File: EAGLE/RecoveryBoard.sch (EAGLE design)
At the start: 54 parts, among them IC1 BD62120AEFJ-E2, Q6 MOSFET-PCH-SOT23-6, U1 STM32F042K6, U10 TPS63070, Y1 ECS-160-10-36Q-ES-TR

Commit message: updated gitignore finally working
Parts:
- added U$5: MP26123DR-LF-Z, U--MP26123DR-LF-Z--LiPo Charger:MP26123DR-LF-Z
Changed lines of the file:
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@@
 </part>
 <part name="GND3" library="supply1" deviceset="GND" device=""/>
+<part name="U$5" library="U--MP26123DR-LF-Z--LiPo Charger" deviceset="MP26123DR-LF-Z" device=""/>
 </parts>
 <sheets>
@@
 <attribute name="DRAWING_NAME" x="469.9" y="19.05" size="2.54" layer="94"/>
 </instance>
-<instance part="VUMB1" gate="1" x="312.42" y="254" smashed="yes">
-<attribute name="VALUE" x="309.88" y="248.92" size="1.778" layer="96" rot="R90"/>
+<instance part="VUMB1" gate="1" x="196.85" y="246.38" smashed="yes">
+<attribute name="VALUE" x="194.31" y="241.3" size="1.778" layer="96" rot="R90"/>
+</instance>
+<instance part="U$5" gate="G$1" x="233.68" y="223.52" smashed="yes">
+<attribute name="NAME" x="233.68" y="226.06" size="0.8128" layer="95" align="center"/>
+<attribute name="VALUE" x="233.68" y="223.52" size="0.8128" layer="96" align="center"/>
 </instance>
 </instances>

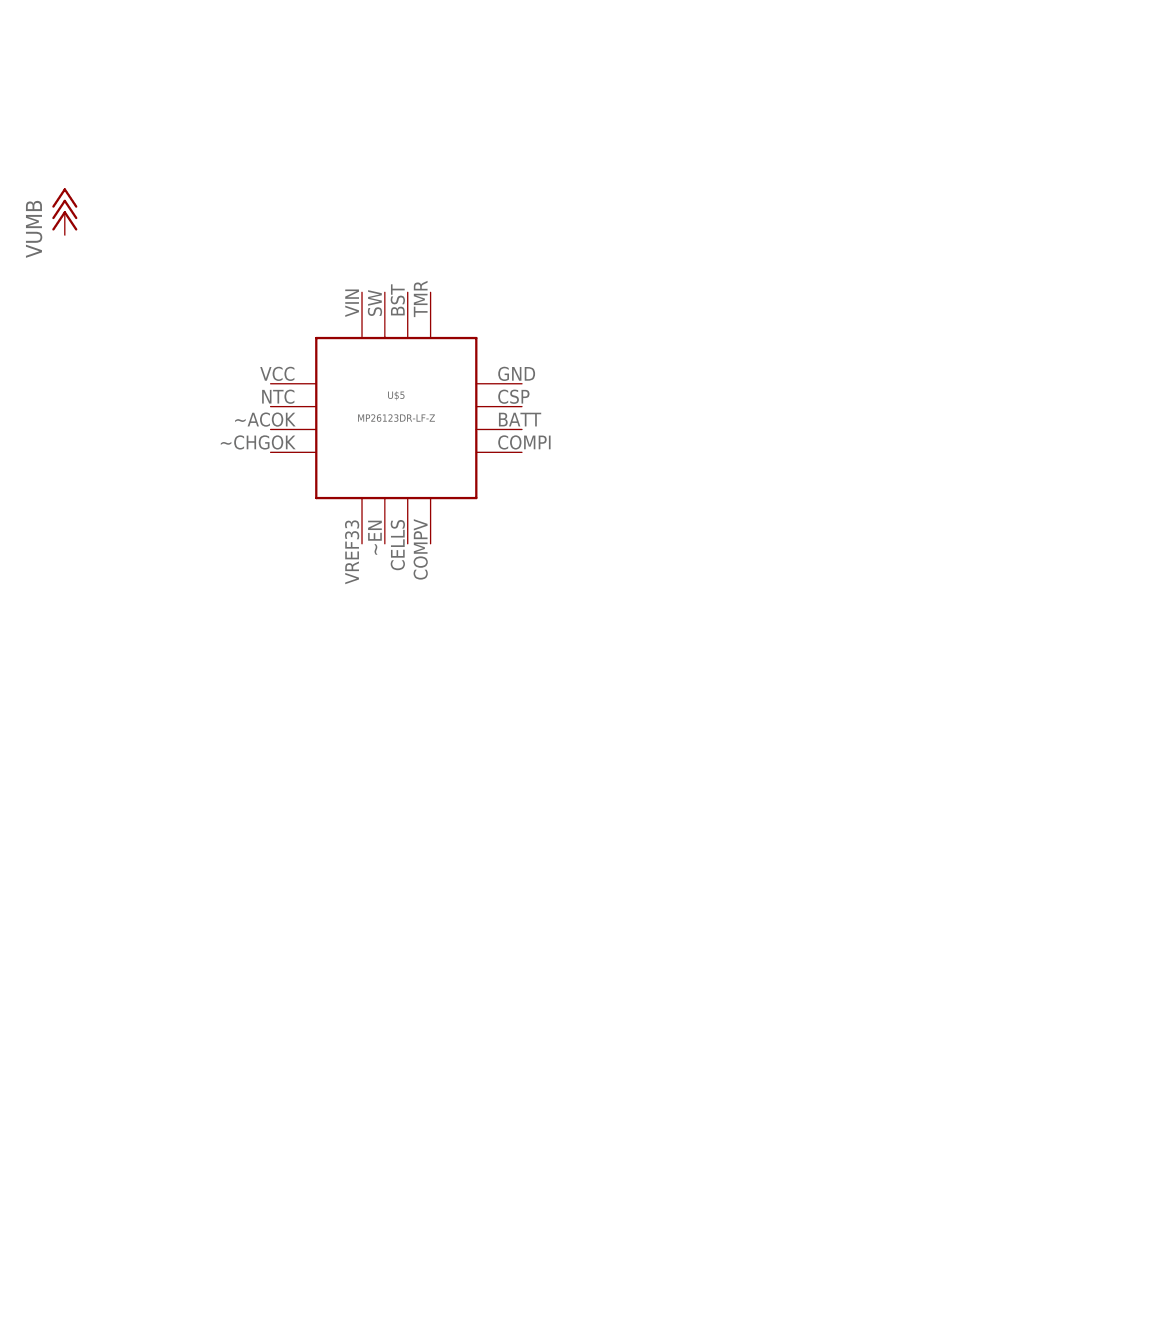
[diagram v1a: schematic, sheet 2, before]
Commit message: updated board to include LiPo charger, and the changes discussed after first design review
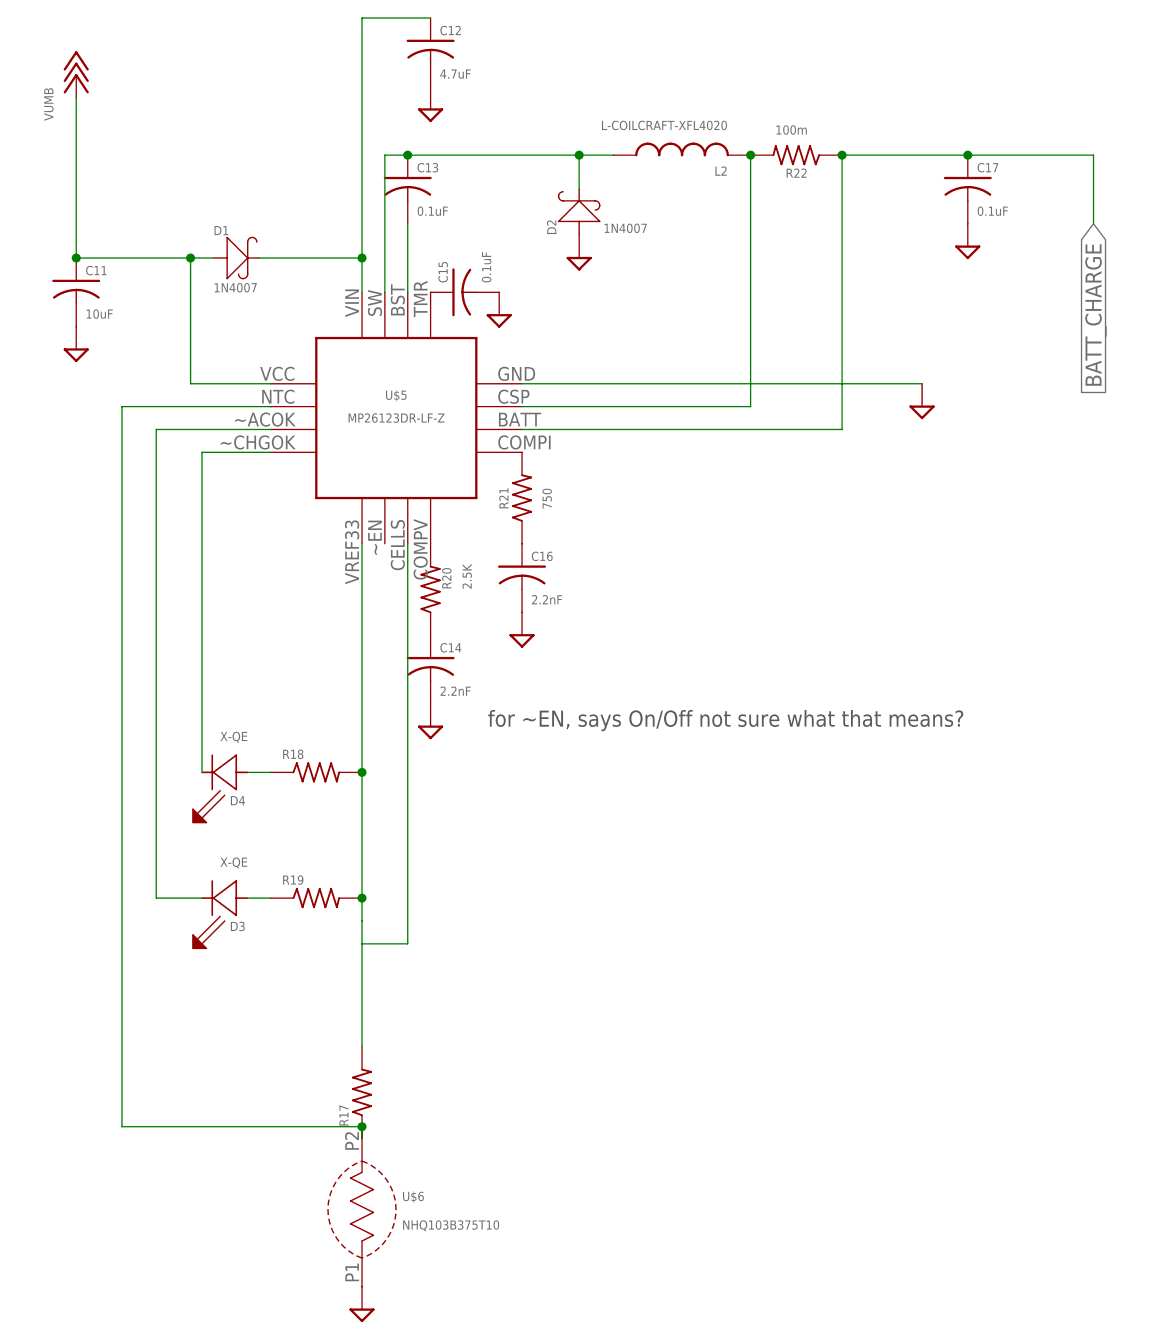
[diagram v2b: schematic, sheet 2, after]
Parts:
- added C11: 10uF, rcl:C-USC0402
- added C12: 4.7uF, rcl:C-USC0402
- added C13, C15, C17: 0.1uF, rcl:C-USC0402
- added C14, C16: 2.2nF, rcl:C-USC0402
- added D1, D2: 1N4007, D-Generic-Schottky-DO-214AC-SMA:DIODE-SCHOTTKY-(DO-214AC)
- added D3, D4: X-QE, D-Cree-XQE-LED:X-QE
- added L2: L-COILCRAFT-XFL4020, L-Coilcraft-XFL4020:L-COILCRAFT-XFL4020
- added R17, R18, R19: (no value), rcl:R-US_R0402
- added R20: 2.5K, rcl:R-US_R0402
- added R21: 750, rcl:R-US_R0402
- added R22: 100m, rcl:R-US_R0402
- added U$6: NHQ103B375T10, R--NHQ103B375T10--Thermistor:NHQ103B375T10
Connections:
- net DMC_ON renamed DCM_ON
- new net N$10: C13.1, D2.-, L2.1, U$5.SW
- new net N$11: C13.2, U$5.BST
- new net N$12: R17.1, U$5.NTC, U$6.P2
- new net N$13: D4.C, U$5.~CHGOK
- new net N$14: R17.2, R18.2, R19.2, U$5.CELLS, U$5.VREF33
- new net N$15: D3.C, U$5.~ACOK
- new net N$16: D3.A, R19.1
- new net N$17: D4.A, R18.1
- new net N$18: R20.2, U$5.COMPV
- new net N$19: C14.1, R20.1
- new net N$20: C15.1, U$5.TMR
- new net N$21: R21.2, U$5.COMPI
- new net N$22: C16.1, R21.1
- new net N$23: L2.2, R22.2, U$5.CSP
- new net N$9: C12.1, D1.-, U$5.VIN
- net +18V: now also C11.1, D1.+, U$5.VCC
- net BATT_CHARGE: now also C17.1, R22.1, U$5.BATT
- net GND: now also C11.2, C12.2, C14.2, C15.2, C16.2, C17.2, D2.+, U$5.GND, U$6.P1
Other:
- note added: "for ~EN, says On/Off not sure what that means?"
- note added: "this wiring is weird...can't name a net for chute and cone"
- note removed: "need umbilical connection"

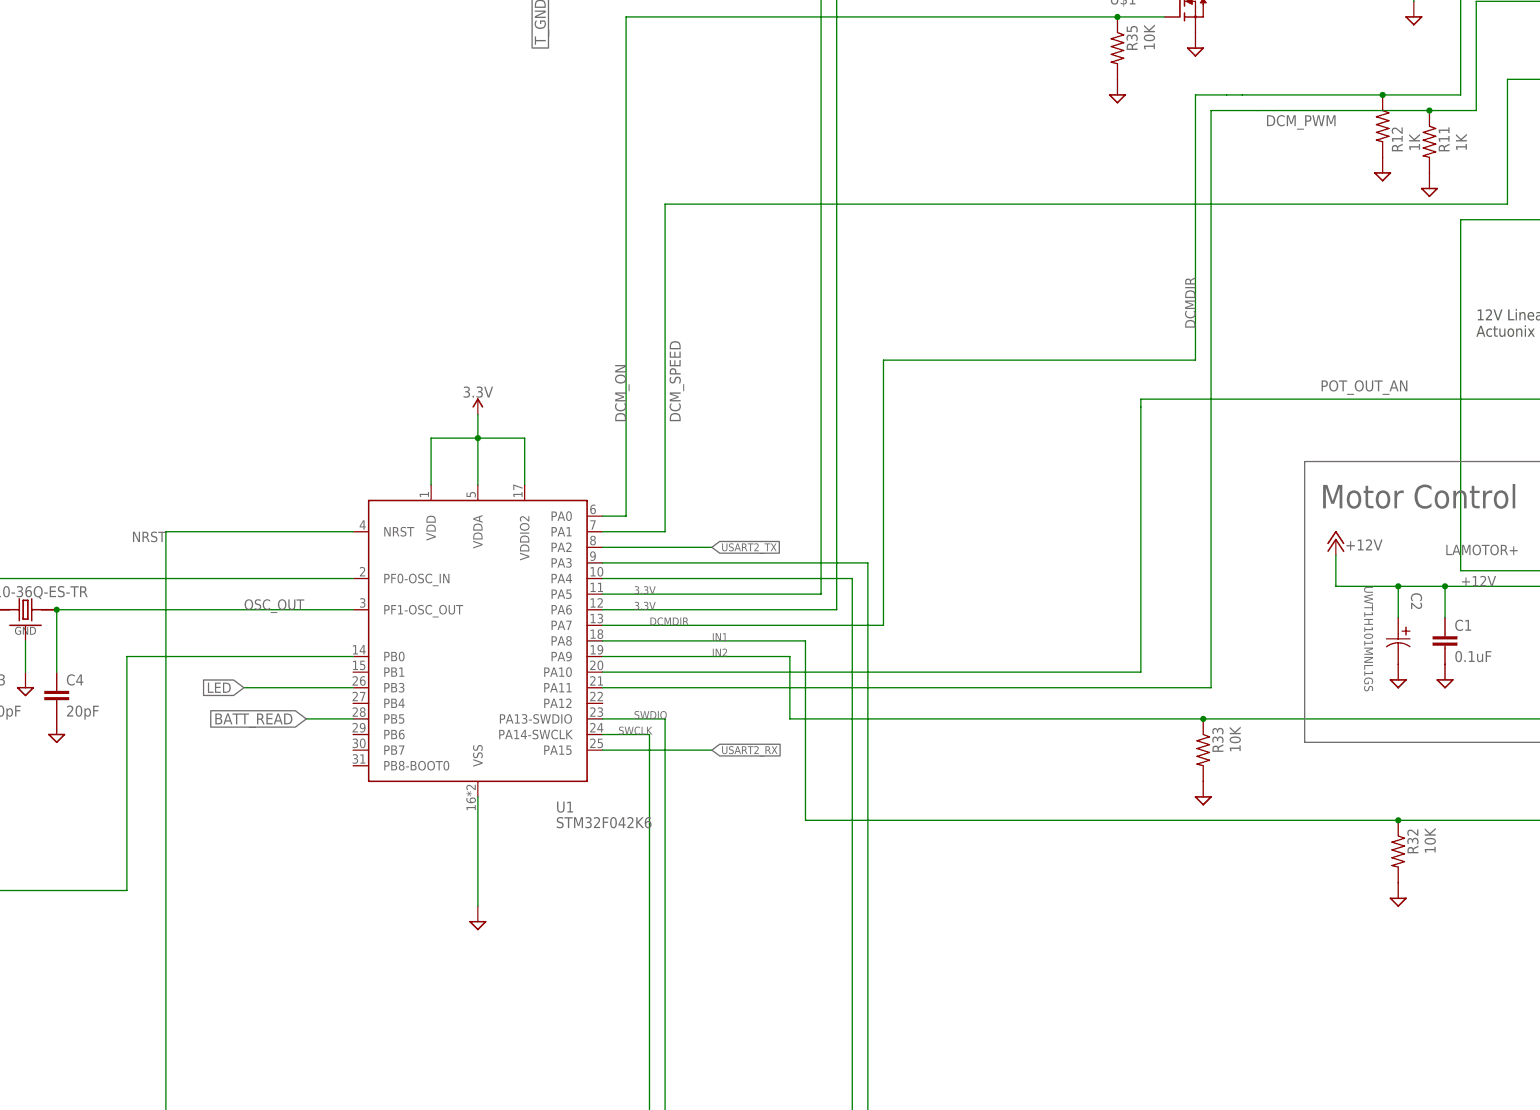
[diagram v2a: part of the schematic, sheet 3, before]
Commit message: updating STM32F0 pins
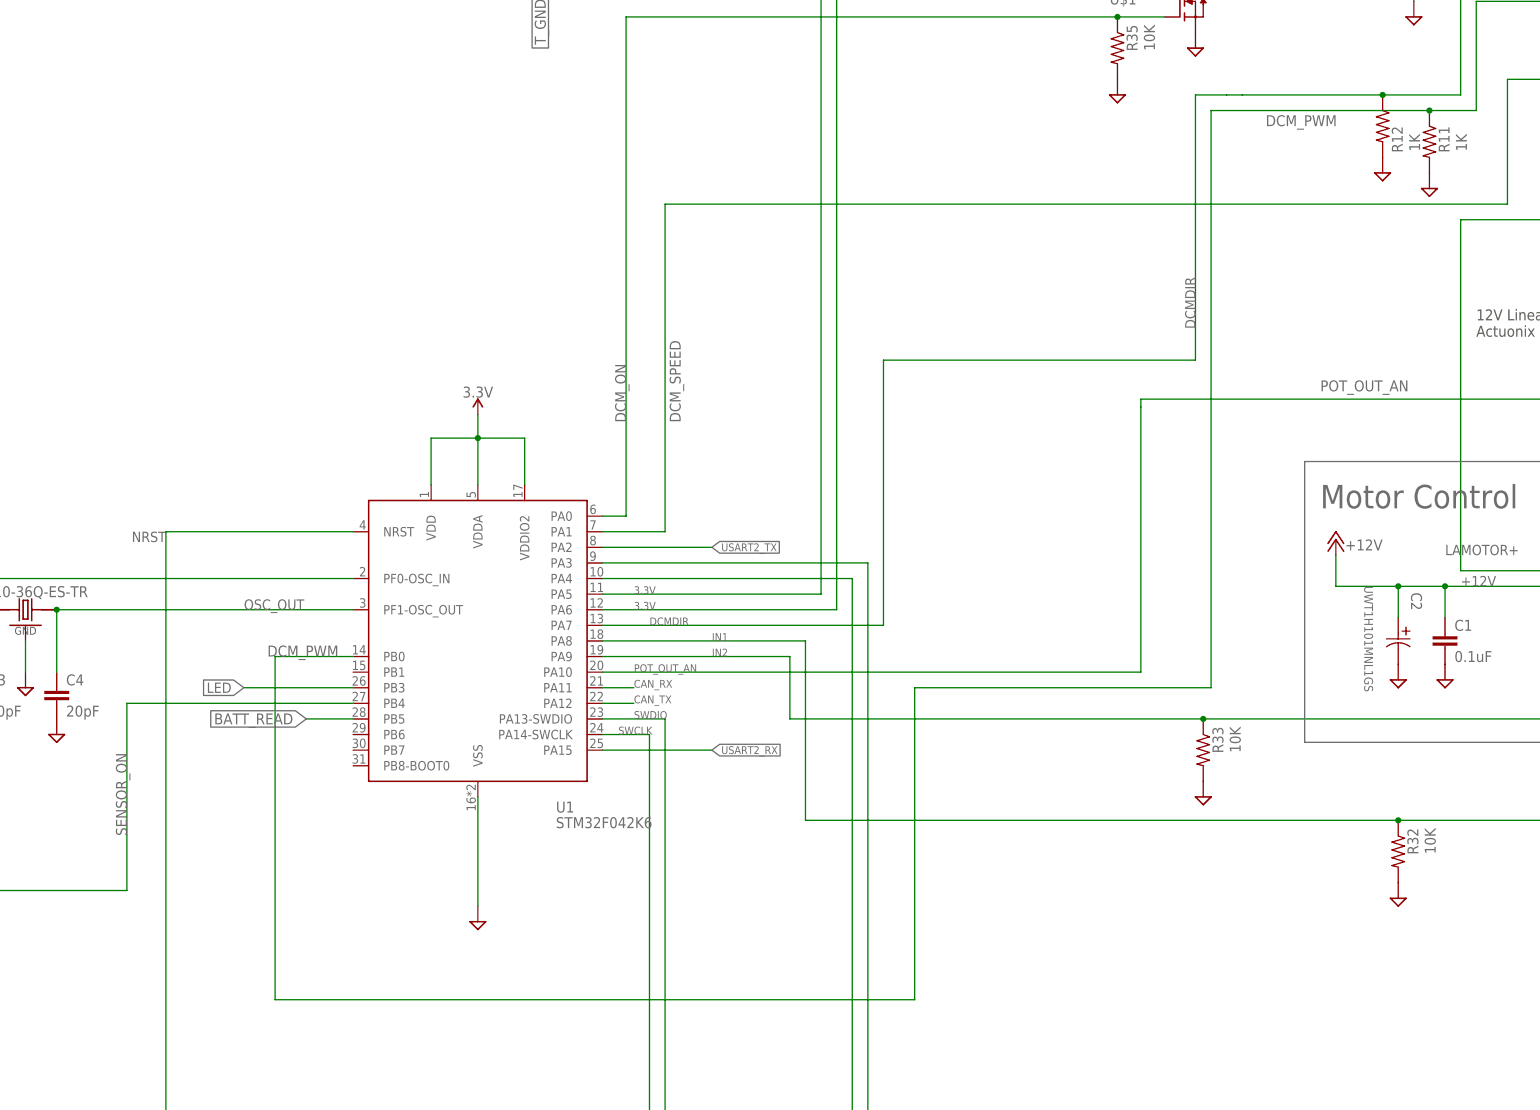
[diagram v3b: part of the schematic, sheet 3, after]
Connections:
- new net CAN_RX: U1.PA11
- new net CAN_TX: U1.PA12
- net DCM_PWM: now also U1.PB0; no longer U1.PA11
- net SENSOR_ON: now also U1.PB4; no longer U1.PB0
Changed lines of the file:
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@@
 <net name="SENSOR_ON" class="0">
 <segment>
-<pinref part="U1" gate="G$1" pin="PB0"/>
-<wire x1="254" y1="182.88" x2="217.17" y2="182.88" width="0.1524" layer="91"/>
-<wire x1="217.17" y1="182.88" x2="217.17" y2="144.78" width="0.1524" layer="91"/>
+<wire x1="217.17" y1="175.26" x2="217.17" y2="144.78" width="0.1524" layer="91"/>
 <wire x1="217.17" y1="144.78" x2="180.34" y2="144.78" width="0.1524" layer="91"/>
 <wire x1="180.34" y1="144.78" x2="180.34" y2="203.2" width="0.1524" layer="91"/>
@@
 <wire x1="71.12" y1="175.26" x2="73.66" y2="175.26" width="0.1524" layer="91"/>
 <junction x="71.12" y="175.26"/>
+<pinref part="U1" gate="G$1" pin="PB4"/>
+<wire x1="254" y1="175.26" x2="217.17" y2="175.26" width="0.1524" layer="91"/>
+<label x="217.17" y="153.67" size="1.778" layer="95" rot="R90"/>
 </segment>
 </net>
@@
 <wire x1="436.88" y1="289.56" x2="436.88" y2="271.78" width="0.1524" layer="91"/>
 <wire x1="436.88" y1="271.78" x2="429.26" y2="271.78" width="0.1524" layer="91"/>
-<pinref part="U1" gate="G$1" pin="PA11"/>
-<wire x1="429.26" y1="271.78" x2="403.86" y2="271.78" width="0.1524" layer="91"/>
-<wire x1="403.86" y1="271.78" x2="401.32" y2="271.78" width="0.1524" layer="91"/>
-<wire x1="294.64" y1="177.8" x2="393.7" y2="177.8" width="0.1524" layer="91"/>
+<wire x1="429.26" y1="271.78" x2="393.7" y2="271.78" width="0.1524" layer="91"/>
 <wire x1="393.7" y1="177.8" x2="393.7" y2="271.78" width="0.1524" layer="91"/>
-<wire x1="393.7" y1="271.78" x2="401.32" y2="271.78" width="0.1524" layer="91"/>
 <label x="402.59" y="269.24" size="1.778" layer="95"/>
 <pinref part="R11" gate="G$1" pin="1"/>
 <junction x="429.26" y="271.78"/>
+<wire x1="393.7" y1="177.8" x2="345.44" y2="177.8" width="0.1524" layer="91"/>
+<wire x1="345.44" y1="177.8" x2="345.44" y2="127" width="0.1524" layer="91"/>
+<wire x1="345.44" y1="127" x2="241.3" y2="127" width="0.1524" layer="91"/>
+<wire x1="241.3" y1="127" x2="241.3" y2="182.88" width="0.1524" layer="91"/>
+<pinref part="U1" gate="G$1" pin="PB0"/>
+<wire x1="241.3" y1="182.88" x2="254" y2="182.88" width="0.1524" layer="91"/>
+<label x="240.03" y="182.88" size="1.778" layer="95"/>
 </segment>
 </net>
@@
 <wire x1="294.64" y1="180.34" x2="382.27" y2="180.34" width="0.1524" layer="91"/>
 <wire x1="382.27" y1="180.34" x2="382.27" y2="223.52" width="0.1524" layer="91"/>
+<label x="299.72" y="180.34" size="1.27" layer="95"/>
 </segment>
 </net>
@@
 </segment>
 </net>
+<net name="CAN_RX" class="0">
+<segment>
+<pinref part="U1" gate="G$1" pin="PA11"/>
+<wire x1="294.64" y1="177.8" x2="299.72" y2="177.8" width="0.1524" layer="91"/>
+<label x="299.72" y="177.8" size="1.27" layer="95"/>
+</segment>
+</net>
+<net name="CAN_TX" class="0">
+<segment>
+<pinref part="U1" gate="G$1" pin="PA12"/>
+<wire x1="294.64" y1="175.26" x2="299.72" y2="175.26" width="0.1524" layer="91"/>
+<label x="299.72" y="175.26" size="1.27" layer="95"/>
+</segment>
+</net>
